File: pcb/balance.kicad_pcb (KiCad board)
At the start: 2 copper layers, 7 x 6 mm, 41 parts, among them J1 Resistive_Touch, J2 JTAG, J3 Conn_01x04_Male, J4 PJ-102AH, J5 UART (Bluetooth), J6 Conn_02x03_Top_Bottom, J7 Conn_02x03_Top_Bottom, M1 Motor_Servo, M2 Motor_Servo, Q1 MMBT3904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

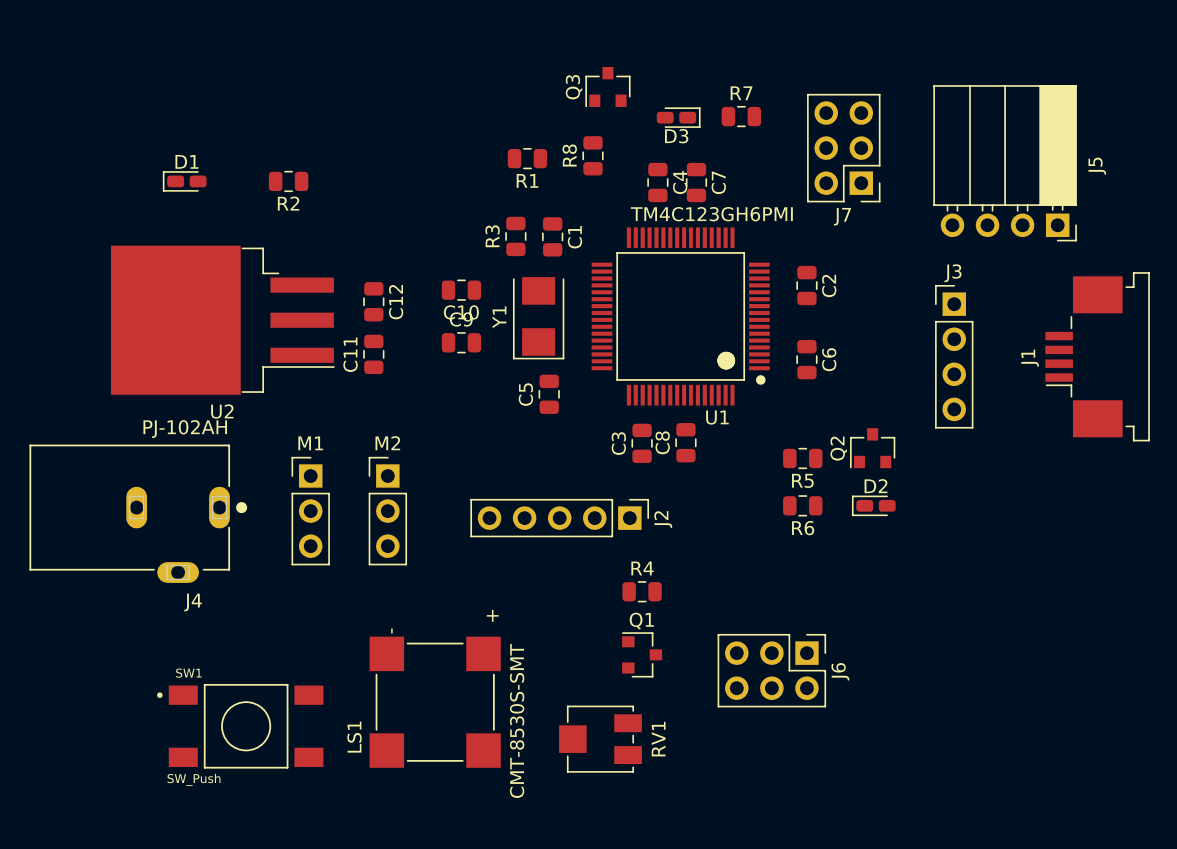
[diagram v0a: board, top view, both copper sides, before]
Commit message: Modify component placement and fix transistor circuits
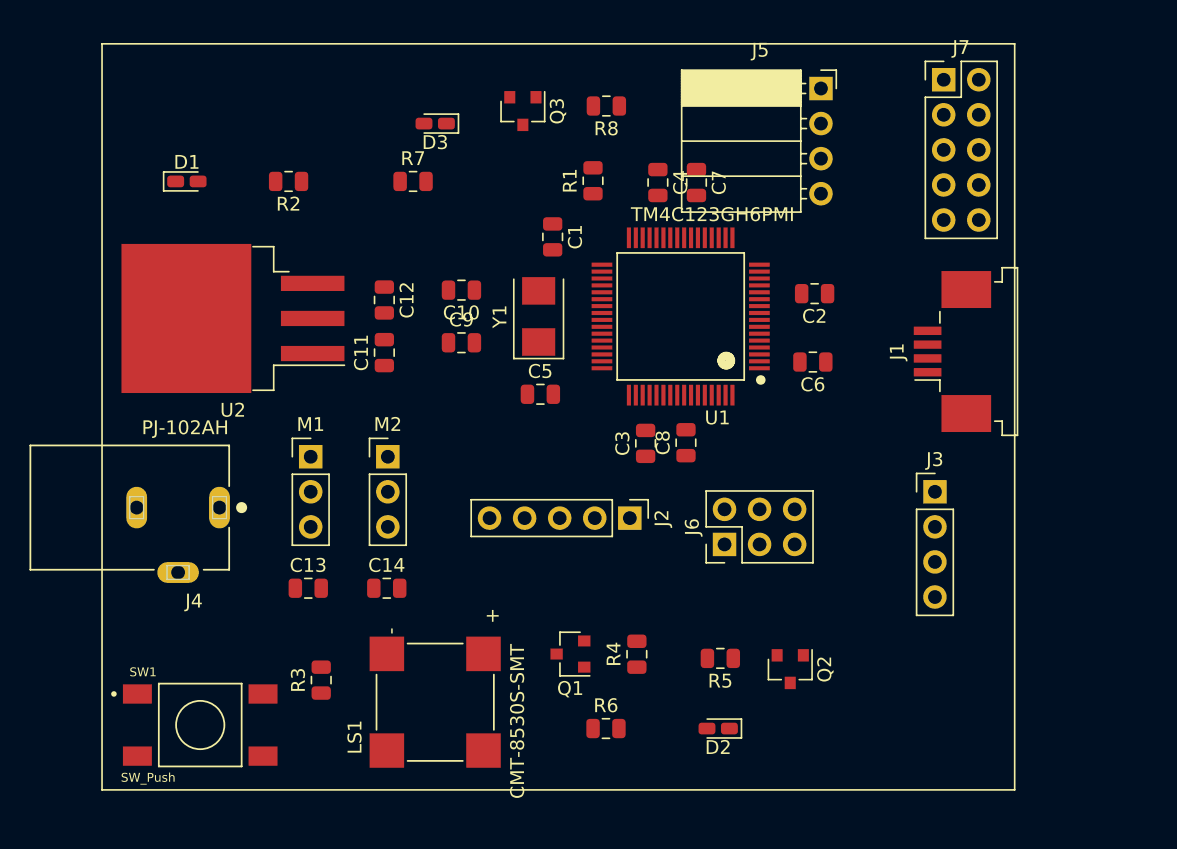
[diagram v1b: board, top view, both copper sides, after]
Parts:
- removed RV1: R_POT_TRIM_500, Potentiometer_SMD:Potentiometer_Bourns_3314J_Vertical
- added C13: 10uF, Capacitor_SMD:C_0805_2012Metric, F.Cu at (96.2, 141.6)
- added C14: 10uF, Capacitor_SMD:C_0805_2012Metric, F.Cu at (101.9, 141.6)
- J7: value Conn_02x03_Top_Bottom -> Conn_02x05_Top_Bottom; footprint Connector_PinHeader_2.54mm:PinHeader_2x03_P2.54mm_Vertical -> Connector_PinHeader_2.54mm:PinHeader_2x05_P2.54mm_Vertical
- moved R3 35.1 mm to (97.2, 148.3)
- moved R7 24.2 mm to (103.8, 112.1)
- moved R6 21.5 mm to (117.8, 151.8), turned to 0 degrees
- moved J5 19.8 mm to (133.3, 105.4), turned to 0 degrees
- moved D2 19.8 mm to (125.9, 151.8), turned to 180 degrees
- moved D3 17.5 mm to (105.4, 108.0)
- moved Q2 17.1 mm to (131.1, 147.5), turned to 270 degrees
- moved R5 15.7 mm to (126.1, 146.7)
- moved J3 13.7 mm to (141.6, 134.6)
- moved J6 9.88 mm to (126.4, 138.4), turned to 90 degrees
- moved J7 9.58 mm to (142.2, 104.8), turned to 0 degrees
- moved J1 9.53 mm to (142.9, 124.5)
- moved Q3 6.40 mm to (111.8, 107.0), turned to 270 degrees
- moved Q1 5.19 mm to (115.2, 146.4), turned to 180 degrees
- moved R1 5.01 mm to (116.8, 112.1), turned to 90 degrees
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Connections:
- J6 pad 1: /PD1 -> /PD0
- J6 pad 2: /PD2 -> /PD1
- J6 pad 3: /PD3 -> /PD2
- J6 pad 4: GND -> /PD3
- LS1 pad N: GND -> Net-(LS1-PadN)
- LS1 pad P: Net-(LS1-PadP) -> +3V3
- Q1 pad 2: Net-(Q1-Pad2) -> GND
- Q1 pad 3: +3V3 -> Net-(LS1-PadN)
- Q2 pad 2: Net-(D2-Pad2) -> GND
- Q2 pad 3: +3V3 -> Net-(D2-Pad1)
- Q3 pad 2: Net-(D3-Pad2) -> GND
- Q3 pad 3: +3V3 -> Net-(D3-Pad1)
- R6 pad 1: Net-(D2-Pad1) -> +3V3
- R6 pad 2: GND -> Net-(D2-Pad2)
- R7 pad 1: Net-(D3-Pad1) -> +3V3
- R7 pad 2: GND -> Net-(D3-Pad2)
- U1 pad 13: (no net) -> /PC7
- U1 pad 14: (no net) -> /PC6
- U1 pad 16: (no net) -> /PC4
- U1 pad 60: (no net) -> /BZZZ
- U1 pad 61: /BZZZ -> /PD0

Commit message: Route the board
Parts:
- added G***: LOGO, pineapple:pineapple, F.Cu at (138.0, 150.0)
- J4: value PJ-102AH -> Barrel_Jack_Switch; footprint PJ-102AH:CUI_PJ-102AH -> Connector_BarrelJack:BarrelJack_CUI_PJ-102AH_Horizontal
- J5: footprint Connector_PinSocket_2.54mm:PinSocket_1x04_P2.54mm_Horizontal -> Connector_PinSocket_2.54mm:PinSocket_1x04_P2.54mm_Vertical
- moved D1 18.4 mm to (105.5, 115.8), turned to 180 degrees
- moved J3 8.61 mm to (145.1, 142.5), turned to 270 degrees
- moved R2 8.18 mm to (101.6, 116.7), turned to 90 degrees
- moved J4 6.47 mm to (89.8, 135.5), turned to 270 degrees
- moved Q2 5.13 mm to (126.0, 147.4), turned to 0 degrees
- moved R5 4.86 mm to (125.0, 141.9), turned to 90 degrees
- moved R6 3.88 mm to (115.1, 149.0)
- moved SW1 3.51 mm to (88.4, 148.0)
- moved R7 3.27 mm to (106.9, 111.2), turned to 90 degrees
- moved J7 3.24 mm to (139.0, 104.9)
- moved D3 3.21 mm to (107.9, 105.9)
- moved Q1 3.00 mm to (115.2, 143.4)
- moved R4 3.00 mm to (120.0, 143.4)
- moved Q3 2.99 mm to (114.7, 107.0)
- moved R8 2.74 mm to (120.5, 107.0), turned to 90 degrees
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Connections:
- J7 pad 8: /PC6 -> /PC5
- U1 pad 15: (no net) -> /PC5
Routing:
- net +3V3: track 0.00 -> 153.6 mm, vias 0 -> 2
- net +5V: track 0.00 -> 87.0 mm, vias 0 -> 2
- net GND: track 0.00 -> 54.2 mm, vias 0 -> 6
- net /RESET: track 0.00 -> 45.1 mm, vias 0 -> 2
- net Net-(J1-Pad4): track 0.00 -> 35.3 mm
- net Net-(J1-Pad3): track 0.00 -> 33.1 mm
- net /Servo0: track 0.00 -> 32.8 mm, vias 0 -> 2
- net Net-(J1-Pad2): track 0.00 -> 32.5 mm
- net Net-(J1-Pad1): track 0.00 -> 30.6 mm
- net /Servo1: track 0.00 -> 28.7 mm, vias 0 -> 2
- net /PA7: track 0.00 -> 24.4 mm, vias 0 -> 2
- net /PA3: track 0.00 -> 23.3 mm
- net /PA5: track 0.00 -> 22.4 mm
- net /BZZZ: track 0.00 -> 20.6 mm
- net /PA6: track 0.00 -> 20.1 mm, vias 0 -> 2
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- added copper zone on F.Cu, net GND
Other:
- board size 7 x 6 mm -> 67 x 55 mm
- net class Default: clearance 0.2 -> 0.127; trace_width 0.25 -> 0.2
- net class Power added: clearance 0.127, trace_width 0.254, via_dia 0.8, via_drill 0.4
- rule trace_clearance: 0.2 -> 0.127
- board text added: "Andrew Jacob Matthew Jiang Joshua Johnson Joseph Ryan"

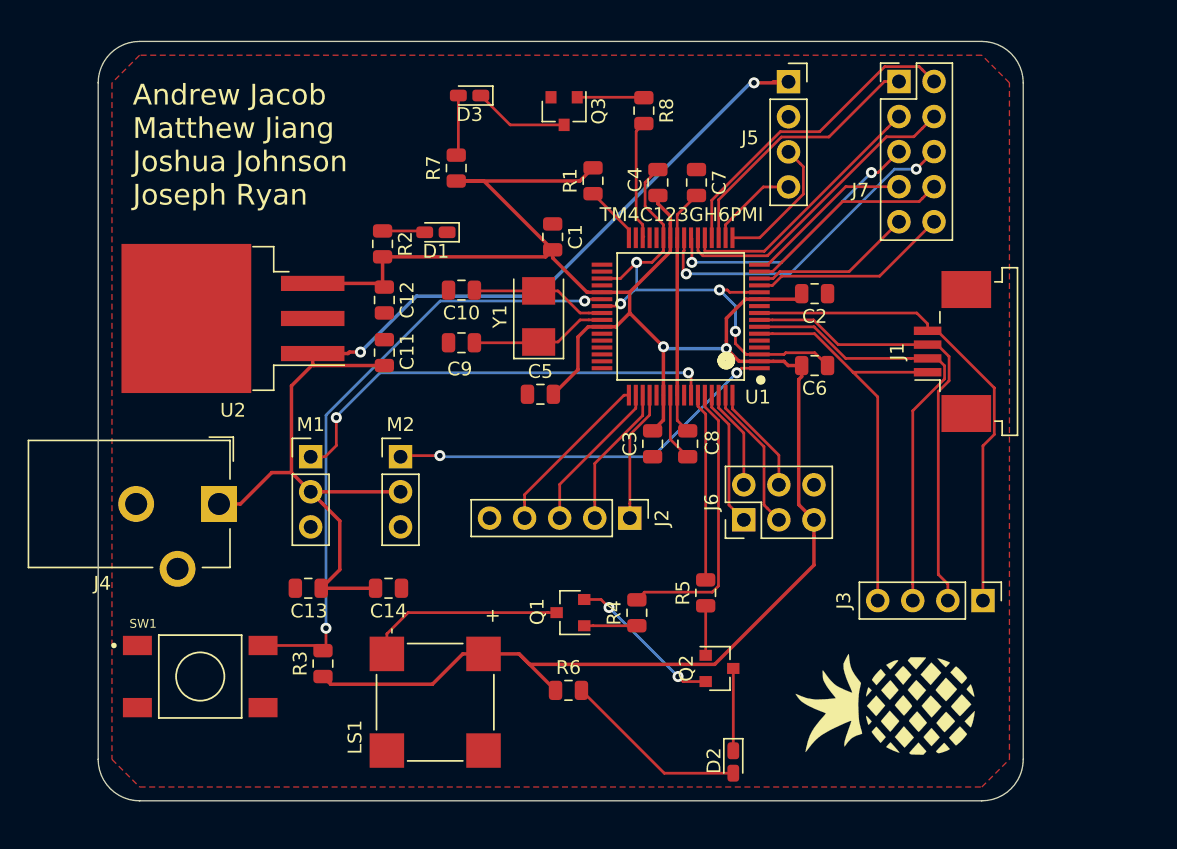
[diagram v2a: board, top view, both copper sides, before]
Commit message: Add mounting holes and remove some vias
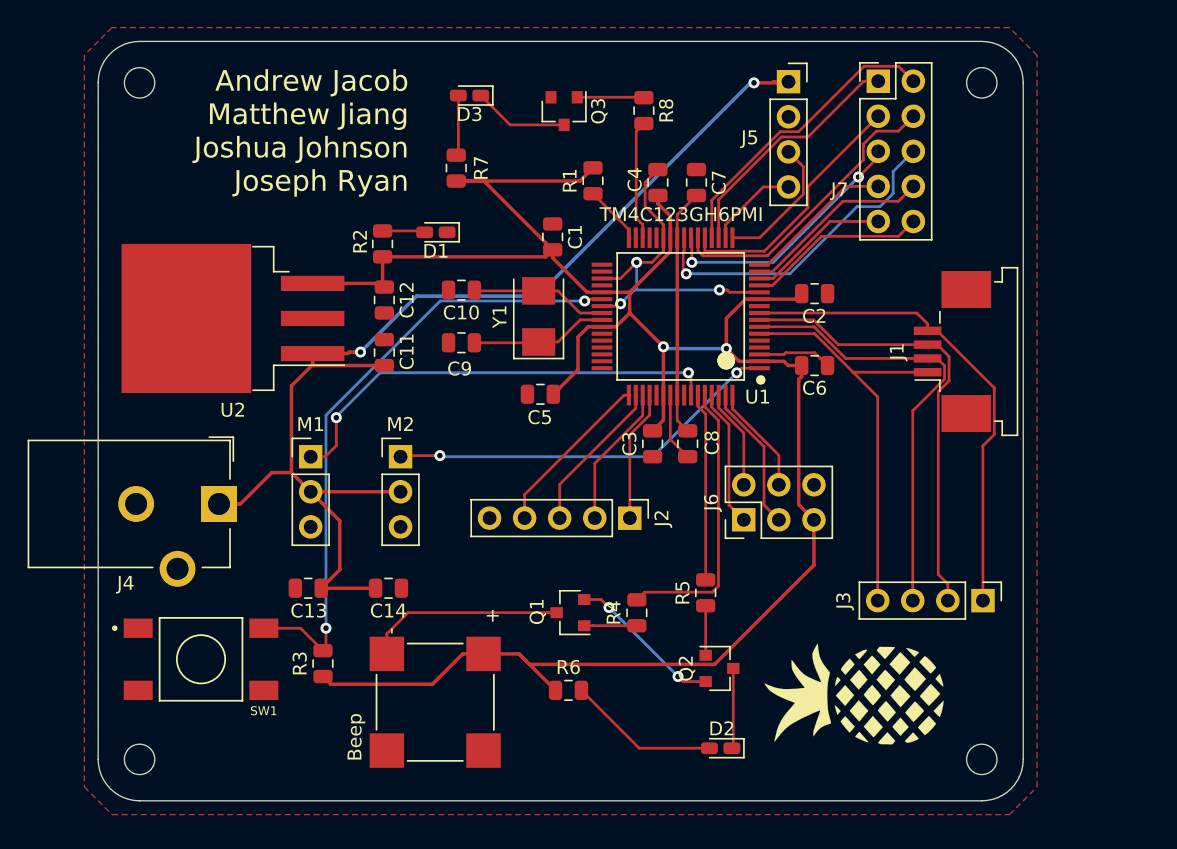
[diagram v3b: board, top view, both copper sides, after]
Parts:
- added REF**: MountingHole_2.2mm_M2, MountingHole:MountingHole_2.2mm_M2, F.Cu at (84.0, 154.0)
- added REF**: MountingHole_2.2mm_M2, MountingHole:MountingHole_2.2mm_M2, F.Cu at (84.0, 105.0)
- added REF**: MountingHole_2.2mm_M2, MountingHole:MountingHole_2.2mm_M2, F.Cu at (145.0, 105.0)
- added REF**: MountingHole_2.2mm_M2, MountingHole:MountingHole_2.2mm_M2, F.Cu at (145.0, 154.0)
- J7: value Conn_02x05_Top_Bottom -> Conn_02x05
- moved G*** 2.37 mm to (135.8, 149.2)
- moved J7 1.50 mm to (137.5, 104.9)
- moved D2 1.35 mm to (126.1, 153.2), turned to 180 degrees
- moved SW1 1.25 mm to (88.5, 146.8)
- renumbered LS1 to Beep
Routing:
- net GND: track 54.2 -> 47.7 mm, vias 6 -> 5
- net Net-(D2-Pad2): track 13.5 -> 11.0 mm
- net /PC4: track 12.5 -> 11.0 mm
- net /PC6: track 11.8 -> 10.3 mm
- net /PC7: track 14.6 -> 13.1 mm
- net /PC5: track 15.2 -> 13.7 mm
- net /PA3: track 23.3 -> 21.8 mm
- net /PA2: track 19.4 -> 17.9 mm
- net /PA6: track 20.1 -> 18.9 mm
- net /RESET: track 45.1 -> 46.1 mm
- net /PA5: track 22.4 -> 21.5 mm
- net /PA4: track 19.1 -> 18.5 mm
- net /PA7: track 24.4 -> 23.8 mm, vias 2 -> 1
